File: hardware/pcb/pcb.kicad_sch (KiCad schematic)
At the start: 6 parts, among them J1 L_GPIO, J2 R_GPIO, J4 USB_C_Receptacle_USB2.0_14P, U1 ESP32-C3-WROOM-02

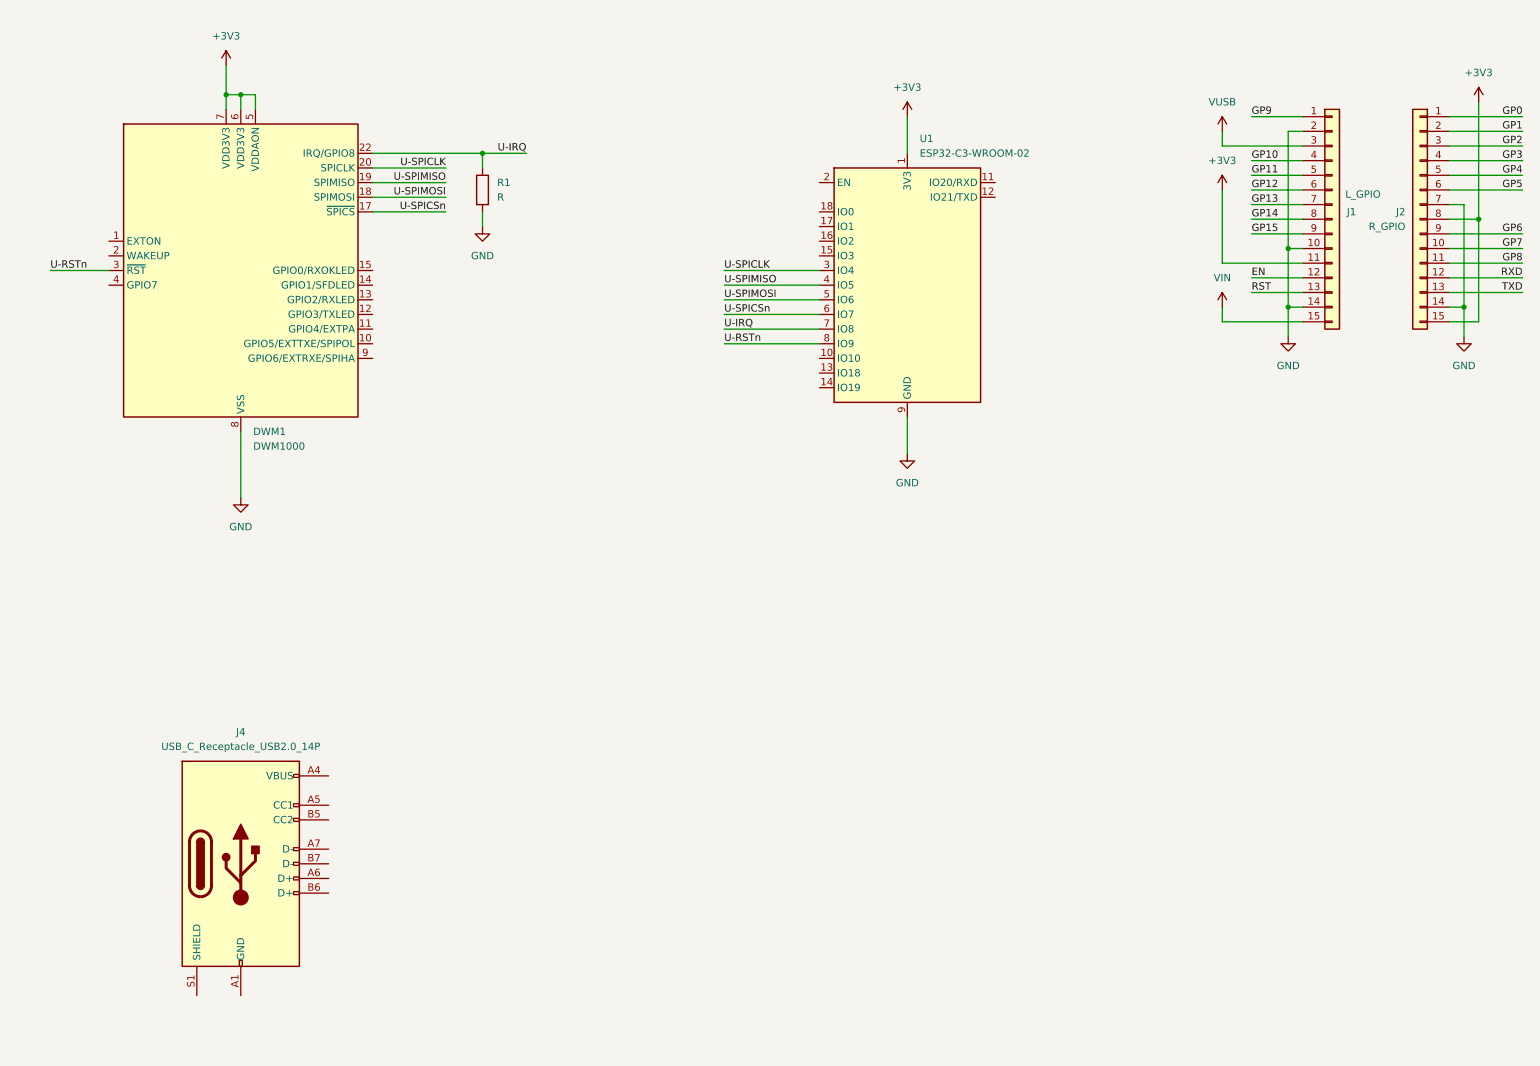
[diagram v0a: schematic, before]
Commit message: PCB: progress on schematic
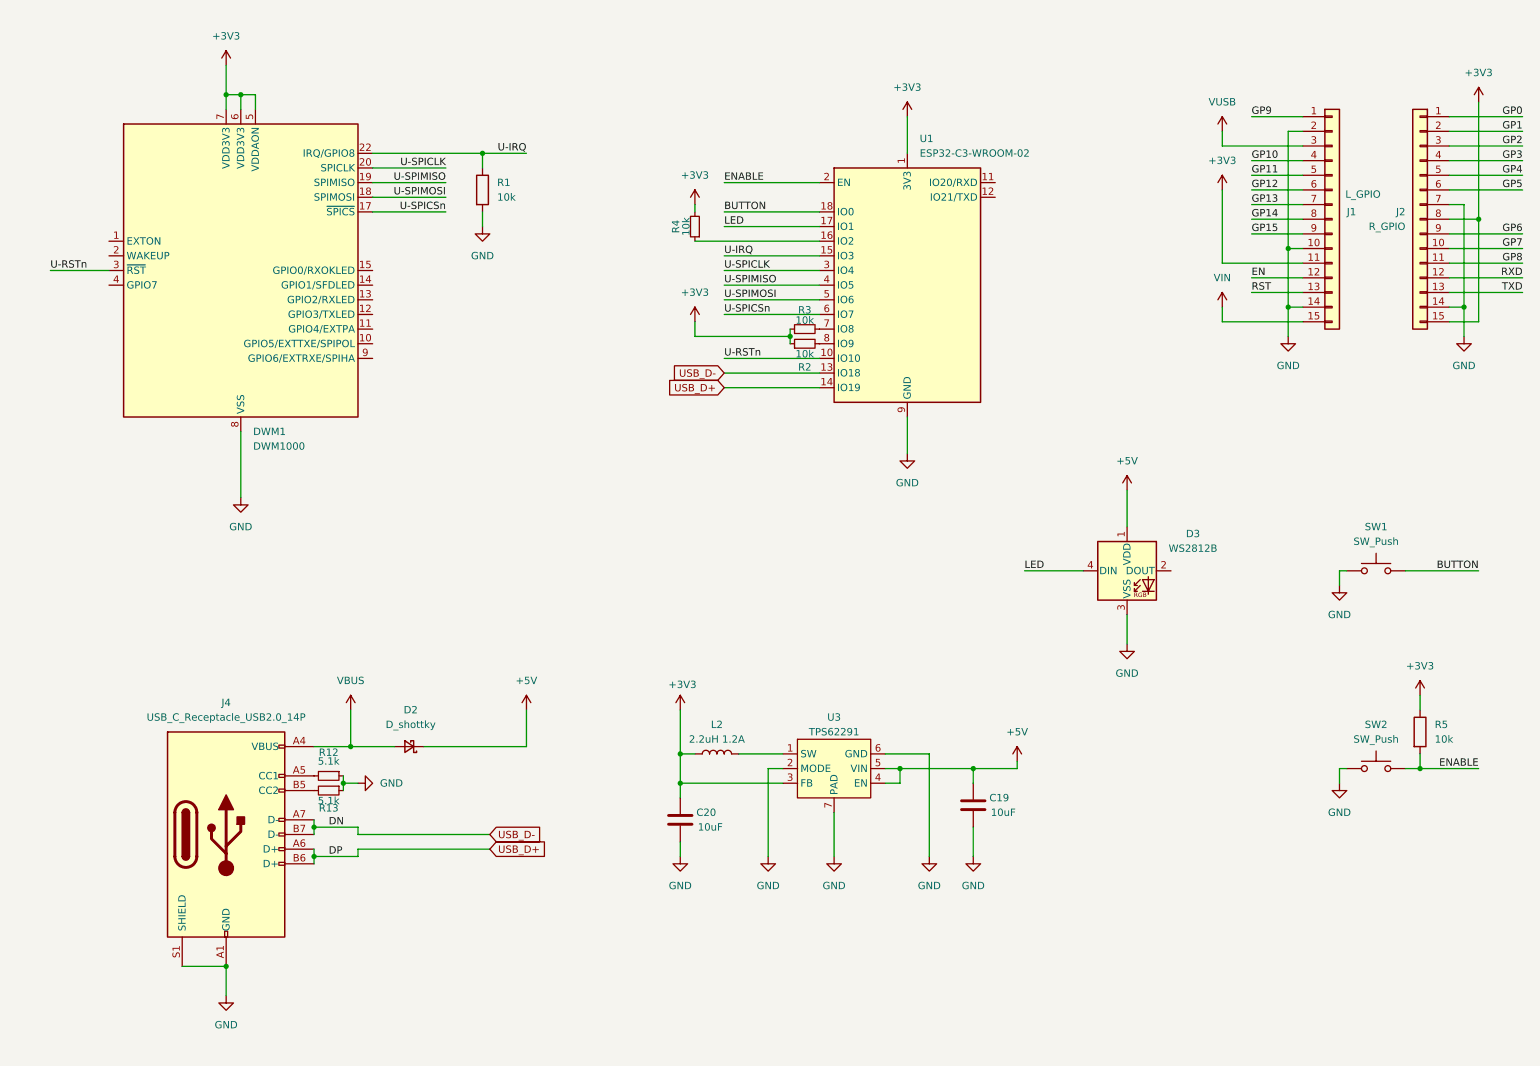
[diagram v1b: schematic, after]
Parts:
- added C19, C20: 10uF, Capacitor_SMD:C_0402_1005Metric, symbol Device:C
- added D2: D_shottky, Diode_SMD:D_SOD-123, symbol Device:D_Schottky_Small
- added D3: WS2812B, LED_SMD:LED_WS2812B_PLCC4_5.0x5.0mm_P3.2mm, symbol LED:WS2812B
- added L2: 2.2uH 1.2A, Inductor_SMD:L_0805_2012Metric, symbol Device:L
- added R12, R13: 5.1k, Resistor_SMD:R_0402_1005Metric, symbol Device:R_Small
- added R2, R3, R4: 10k, Resistor_SMD:R_0402_1005Metric, symbol Device:R_Small
- added R5: 10k, Resistor_SMD:R_0402_1005Metric, symbol Device:R
- added SW1, SW2: SW_Push, Button_Switch_THT:SW_PUSH_6mm, symbol Switch:SW_Push
- added U3: TPS62291, Package_SON:WSON-6-1EP_2x2mm_P0.65mm_EP1x1.6mm_ThermalVias, symbol Sisyphus:TPS62293
- J4: footprint (none) -> Connector_USB:USB_C_Receptacle_G-Switch_GT-USB-7010ASV; LCSC Part (none) -> https://lcsc.com/product-detail/USB-Connectors_G-Switch-GT-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
- R1: value R -> 10k; footprint (none) -> Resistor_SMD:R_0402_1005Metric
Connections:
- net +3V3: now also C20.1, L2.1, R2.1, R3.1, R4.2, R5.1, U3.3 (FB)
- net GND: now also J4.A1 (GND), J4.A12 (GND), J4.B1 (GND), J4.B12 (GND), J4.S1 (SHIELD), C19.2, C20.2, D3.3 (VSS), R12.1, R13.1, SW1.1, SW2.1, U3.2 (MODE), U3.6 (GND), U3.7 (PAD)
- net U-IRQ: now also U1.15 (IO3); no longer U1.7 (IO8)
- net U-RSTn: now also U1.10 (IO10); no longer U1.8 (IO9)
- net VBUS: now reaches J4.A4 (VBUS), J4.A9 (VBUS), J4.B4 (VBUS), J4.B9 (VBUS)
- net VBUS: now also D2.2 (A)
- net at J4.A5 (CC1): now also R12.2
- net USB_D+: now reaches J4.A6 (D+)
- net USB_D+: now also J4.B6 (D+), U1.14 (IO19)
- net USB_D-: now reaches J4.A7 (D-)
- net USB_D-: now also J4.B7 (D-), U1.13 (IO18)
- net at J4.B5 (CC2): now also R13.2
- net at U1.16 (IO2): now also R4.1
- net LED: now reaches U1.17 (IO1)
- net LED: now also D3.4 (DIN)
- net BUTTON: now reaches U1.18 (IO0)
- net BUTTON: now also SW1.2
- net ENABLE: now reaches U1.2 (EN)
- net ENABLE: now also R5.2, SW2.2
- new net: R3.2, U1.7 (IO8)
- new net: R2.2, U1.8 (IO9)
- new net: L2.2, U3.1 (SW)
- new net +5V: C19.1, D2.1 (K), D3.1 (VDD), U3.4 (EN), U3.5 (VIN)

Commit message: finished schematic and routed pcb
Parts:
- added D1: TXLED, LED_SMD:LED_0402_1005Metric, symbol Device:LED_Small
- added D4: RXLED, LED_SMD:LED_0402_1005Metric, symbol Device:LED_Small
- added D5: SFDLED, LED_SMD:LED_0402_1005Metric, symbol Device:LED_Small
- added D6: RXOKLED, LED_SMD:LED_0402_1005Metric, symbol Device:LED_Small
- added R6, R7, R8, R9: R_Small, Resistor_SMD:R_0402_1005Metric, symbol Device:R_Small
- SW1: value SW_Push -> MODE
- SW2: value SW_Push -> RESET
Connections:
- net VUSB is gone; now on net +5V: J1.3 (Pin_3)
- net GND: now also D1.1 (K), D4.1 (K), D5.1 (K), D6.1 (K)
- net RXD: now also U1.11 (IO20/RXD)
- net TXD: now also U1.12 (IO21/TXD)
- net TXLED: now reaches DWM1.12 (GPIO3/TXLED)
- net TXLED: now also R6.2
- net RXLED: now reaches DWM1.13 (GPIO2/RXLED)
- net RXLED: now also R7.2
- net SFDLED: now reaches DWM1.14 (GPIO1/SFDLED)
- net SFDLED: now also R8.2
- net RXOKLED: now reaches DWM1.15 (GPIO0/RXOKLED)
- net RXOKLED: now also R9.2
- new net: D6.2 (A), R9.1
- new net: D1.2 (A), R6.1
- new net: D4.2 (A), R7.1
- new net: D5.2 (A), R8.1
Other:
- note added: "BUTTON"
- note added: "DWM1000"
- note added: "DWM1000 STATUS LED"
- note added: "ESP32"
- note added: "ESP32 STATUS LED"
- note added: "HEADER CONNECTOR"
- note added: "RESET"
- note added: "STEPDOWN"
- note added: "USB-C"
- moved on the sheet: C19, C20, D2, D3, DWM1, J1, J2, J4, L2, R1, R12, R13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

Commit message: PCB progress
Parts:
- D2: Shop link (none) -> https://www.lcsc.com/product-detail/C22374920.html?s_z=n_D_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
- D3: Shop link (none) -> https://www.lcsc.com/product-detail/C114586.html?s_z=n_WS28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
- DWM1: Shop link (none) -> https://www.aliexpress.com/item/1005006968042289.html?spm=a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
- J1, J2: Shop link (none) -> kus
- J4: Shop link (none) -> https://www.lcsc.com/product-detail/C5362630.html?s_z=n_USB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
- L2: Shop link (none) -> https://www.lcsc.com/product-detail/C281115.html?s_z=n_L_08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
- SWITCH1: renamed from SW1; Shop link (none) -> https://www.lcsc.com/product-detail/C393938.html?s_z=n_SW%2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
- SWITCH2: renamed from SW2; Shop link (none) -> https://www.lcsc.com/product-detail/C393938.html?s_z=n_SW%2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
- U1: Shop link (none) -> https://www.lcsc.com/product-detail/C2934560.html?s_z=n_ESP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
- U3: Shop link (none) -> https://www.lcsc.com/product-detail/C52772.html?s_z=n_TPS62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

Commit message: PCB progress
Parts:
- C19, C20: Shop link (none) -> https://www.lcsc.com/product-detail/C315248.html?s_z=n_C%25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
- R1, R2, R3, R4, R5: Shop link (none) -> https://www.lcsc.com/product-detail/C2936656.html?s_z=n_R%2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
- R12, R13: Shop link (none) -> https://www.lcsc.com/product-detail/C413002.html?s_z=n_R%25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
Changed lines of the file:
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@@
 			)
 		)
-		(property "Shop link" ""
+		(property "Shop link" "https://www.lcsc.com/product-detail/C2936656.html?s_z=n_R%252010K%25200402"
 			(at 153.67 63.5 90)
 			(effects
@@
 			)
 		)
-		(property "Shop link" ""
+		(property "Shop link" "https://www.lcsc.com/product-detail/C315248.html?s_z=n_C%25200402%252010%2520uf"
 			(at 97.79 171.45 0)
 			(effects
@@
 			)
 		)
-		(property "Shop link" ""
+		(property "Shop link" "https://www.lcsc.com/product-detail/C2936656.html?s_z=n_R%252010K%25200402"
 			(at 153.67 66.04 90)
 			(effects
@@
 			)
 		)
-		(property "Shop link" ""
+		(property "Shop link" "https://www.lcsc.com/product-detail/C315248.html?s_z=n_C%25200402%252010%2520uf"
 			(at 148.59 168.91 0)
 			(effects
@@
 			)
 		)
-		(property "Shop link" ""
+		(property "Shop link" "https://www.lcsc.com/product-detail/C2936656.html?s_z=n_R%252010K%25200402"
 			(at 134.62 45.72 90)
 			(effects
@@
 			)
 		)
-		(property "Shop link" ""
+		(property "Shop link" "https://www.lcsc.com/product-detail/C413002.html?s_z=n_R%25205.1K%25200402"
 			(at 50.8 147.32 90)
 			(effects
@@
 			)
 		)
-		(property "Shop link" ""
+		(property "Shop link" "https://www.lcsc.com/product-detail/C413002.html?s_z=n_R%25205.1K%25200402"
 			(at 50.8 149.86 90)
 			(effects
@@
 			)
 		)
-		(property "Shop link" ""
+		(property "Shop link" "https://www.lcsc.com/product-detail/C2936656.html?s_z=n_R%252010K%25200402"
 			(at 260.35 147.32 0)
 			(effects
@@
 			)
 		)
-		(property "Shop link" ""
+		(property "Shop link" "https://www.lcsc.com/product-detail/C2936656.html?s_z=n_R%252010K%25200402"
 			(at 97.79 46.99 0)
 			(effects

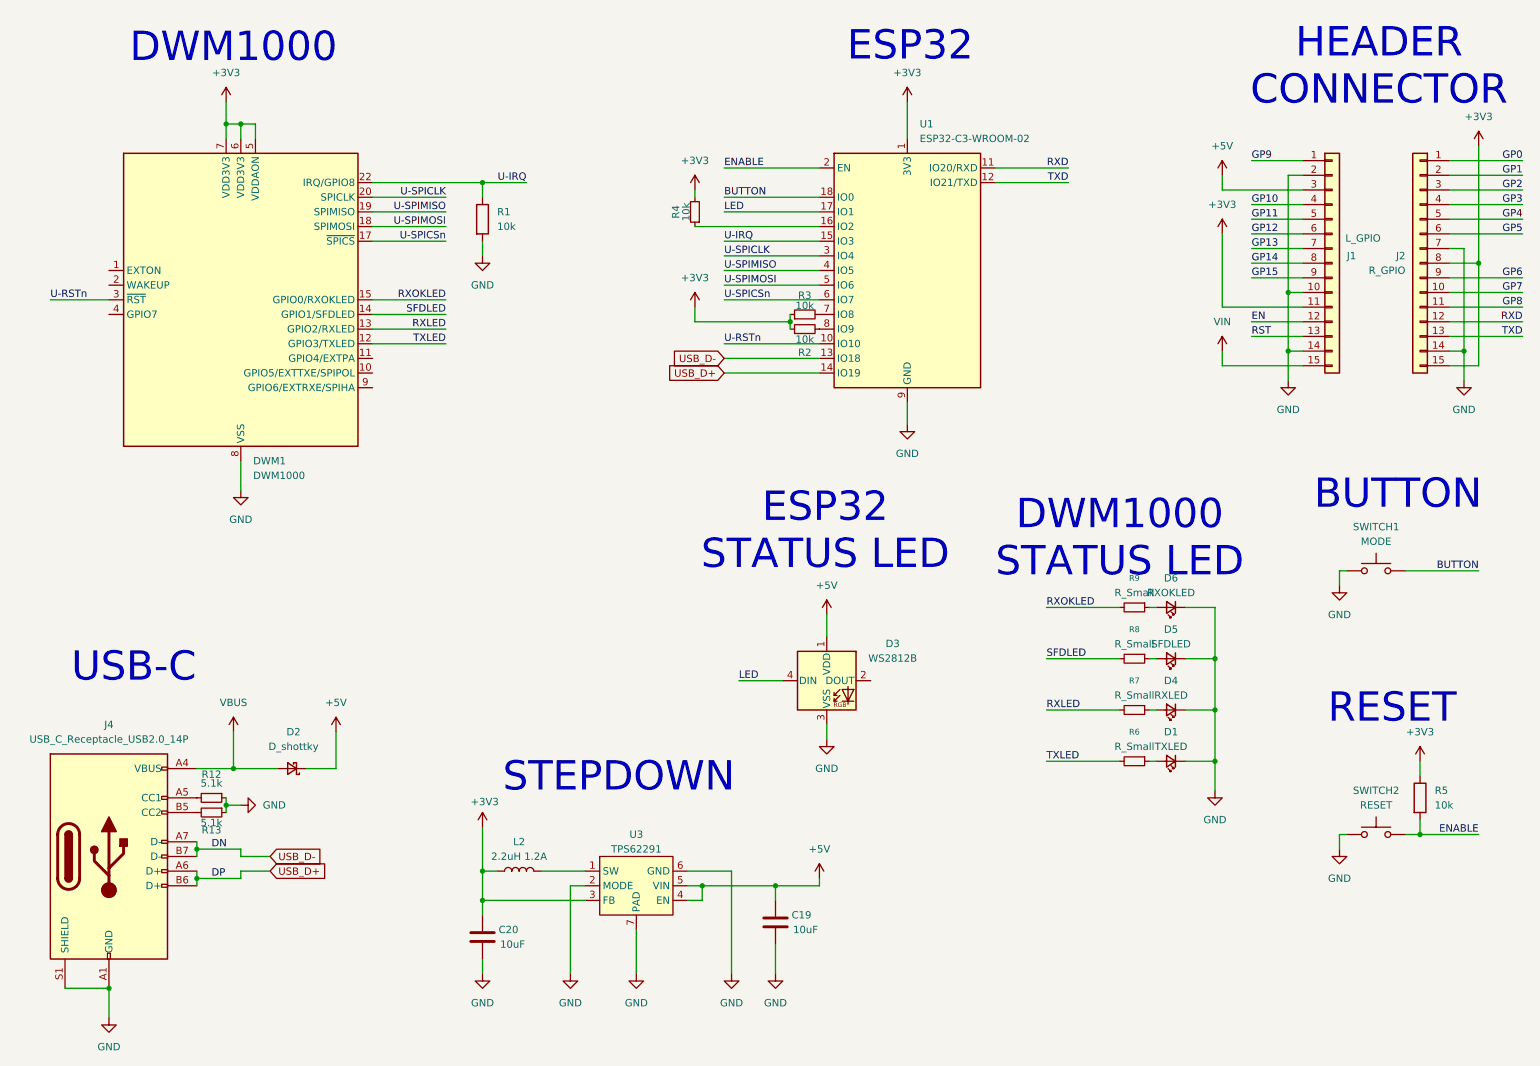
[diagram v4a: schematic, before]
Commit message: added LCSC parts ids for assembly
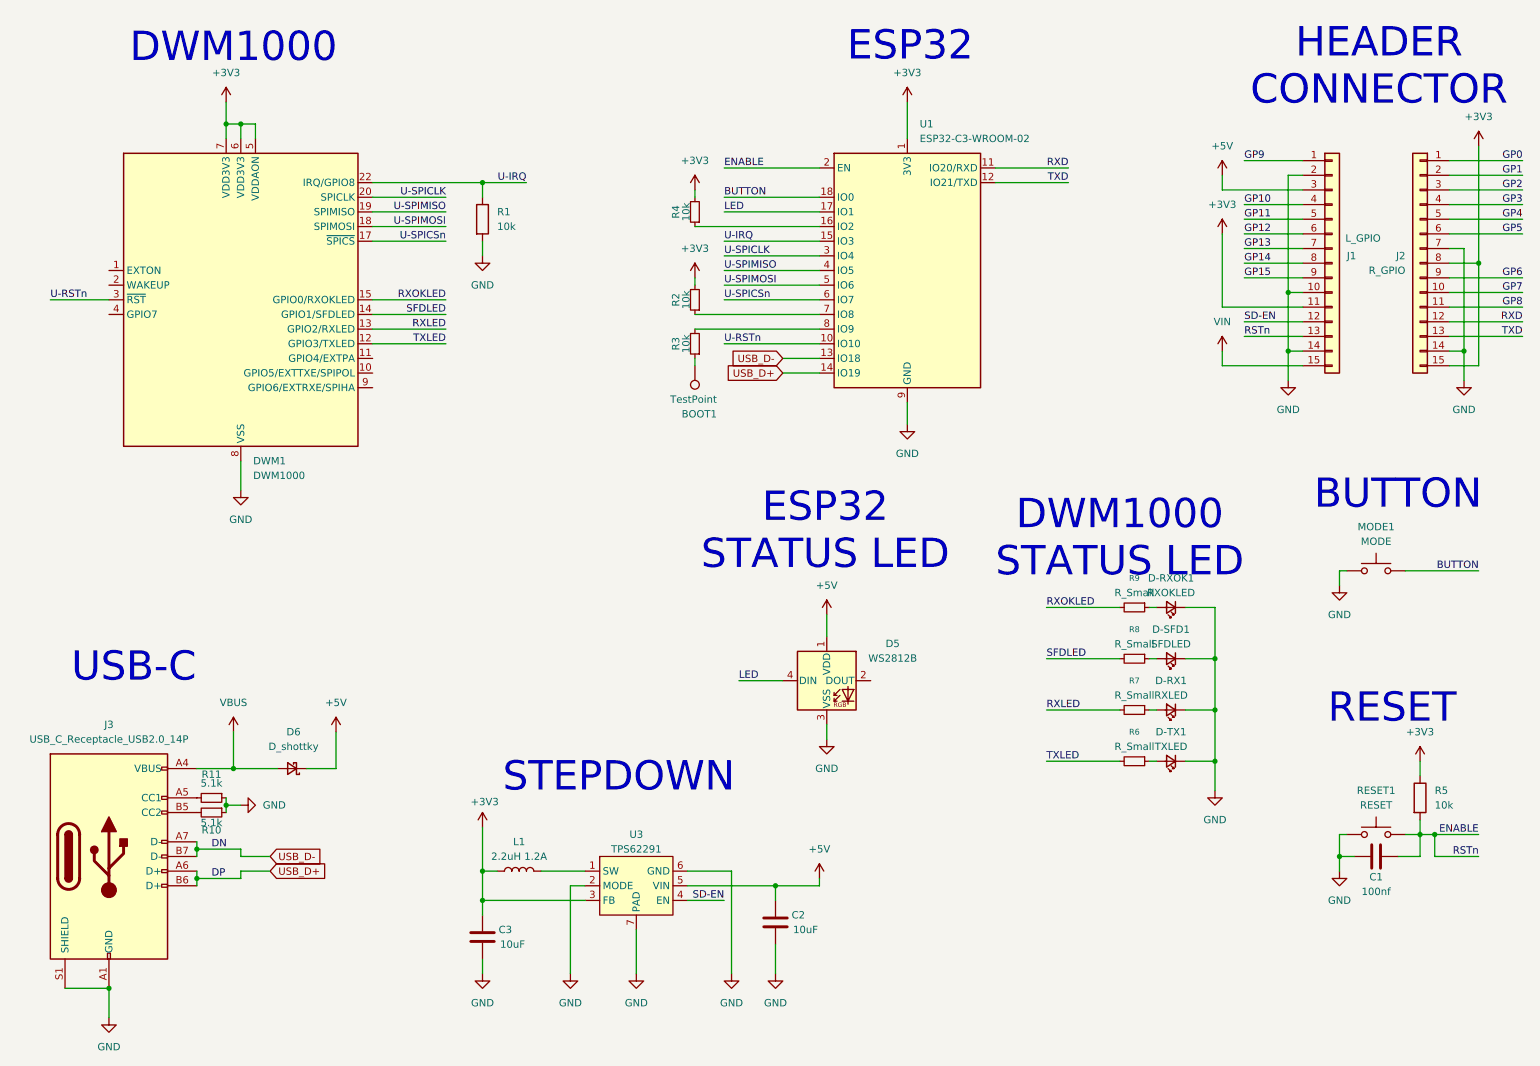
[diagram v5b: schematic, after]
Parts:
- added BOOT1: TestPoint, TestPoint:TestPoint_Pad_2.0x2.0mm, symbol Connector:TestPoint
- added C1: 100nf, Capacitor_SMD:C_0402_1005Metric, symbol Device:C
- C2: renamed from C19; LCSC Part (none) -> C315248
- C3: renamed from C20; LCSC Part (none) -> C315248
- D5: renamed from D3; LCSC Part (none) -> C114586
- D6: renamed from D2; LCSC Part https://lcsc.com/product-detail/Schottky-Diodes_FUXINSEMI-M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 -> C22374920
- J3: renamed from J4; LCSC Part https://lcsc.com/product-detail/USB-Connectors_G-Switch-GT-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 -> C5362630
- L1: renamed from L2; LCSC Part (none) -> C281115
- MODE1: renamed from SWITCH1; LCSC Part (none) -> C393938
- R1, R2, R3, R4, R5: LCSC Part (none) -> C2936656
- R10: renamed from R13; LCSC Part (none) -> C413002
- R11: renamed from R12; LCSC Part (none) -> C413002
- RESET1: renamed from SWITCH2; LCSC Part (none) -> C393938
- U1: LCSC Part (none) -> C2934560
- U3: LCSC Part https://lcsc.com/product-detail/DC-DC-Converters_Texas-Inst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 -> C52772
- renumbered D4 to D-RX1, D6 to D-RXOK1, D5 to D-SFD1, D1 to D-TX1
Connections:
- net RST is gone; now on net ENABLE: J1.13 (Pin_13)
- net +3V3: now also R2.2; no longer R2.1, R3.1
- net +5V: no longer U3.4 (EN)
- net ENABLE: now also C1.1
- net GND: now also C1.2
- net at U1.7 (IO8): now also R2.1; no longer R3.2
- net at U1.8 (IO9): now also R3.2; no longer R2.2
- net EN renamed SD-EN
- net SD-EN: now also U3.4 (EN)
- new net: BOOT1.1, R3.1

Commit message: I dont remeber, something with PCB :)
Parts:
- BOOT1: footprint TestPoint:TestPoint_Pad_2.0x2.0mm -> TestPoint:TestPoint_Pad_D1.5mm
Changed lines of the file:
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@@
 			)
 		)
-		(property "Footprint" "TestPoint:TestPoint_Pad_2.0x2.0mm"
+		(property "Footprint" "TestPoint:TestPoint_Pad_D1.5mm"
 			(at 129.54 72.39 0)
 			(effects
